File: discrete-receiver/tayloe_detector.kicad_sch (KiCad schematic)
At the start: 30 parts, among them U1 SN74CBT3253DBQR, U2 OPA1612AxD, U3 OPA1612AxD

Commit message: Fixed PCB component rotation offsets
A few components needed to get a rotation offset for JLCPCB production. Also more silkscreen content was added.
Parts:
- U1: Rotation Offset (none) -> 270
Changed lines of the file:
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@@
+			)
+		)
+		(property "Rotation Offset" "270"
+			(at 82.55 102.87 0)
+			(hide yes)
+			(show_name no)
+			(do_not_autoplace no)
+			(effects
+				(font
+					(size 1.27 1.27)
+				)
 			)
 		)

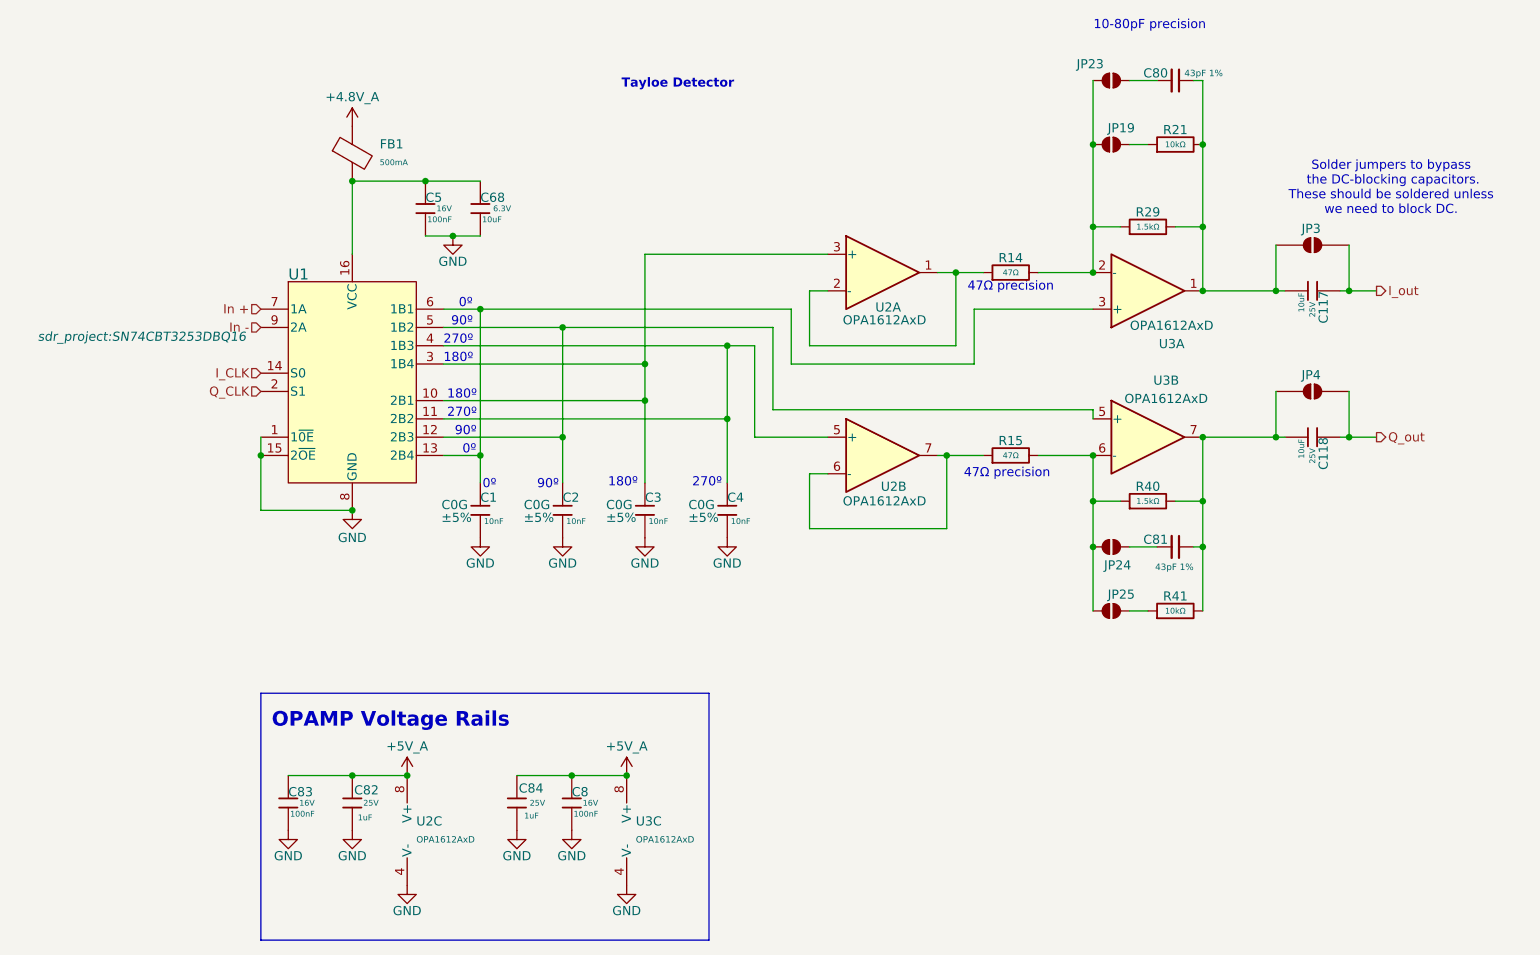
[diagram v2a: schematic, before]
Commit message: Made an edit and fixed isolated power bus in schematic&PCB
The +5V_A bus should not have been used for power in the Tayloe Detector. This was replaced with +4.8V_A in the schematic, the fix was implemented in the PCB, and that bus was connected to the +4.8V_A source.

The edit made was the making JP3 and JP4 in series with C117 & C118 rather than being in series. This change was made in both the schematic and PCB.
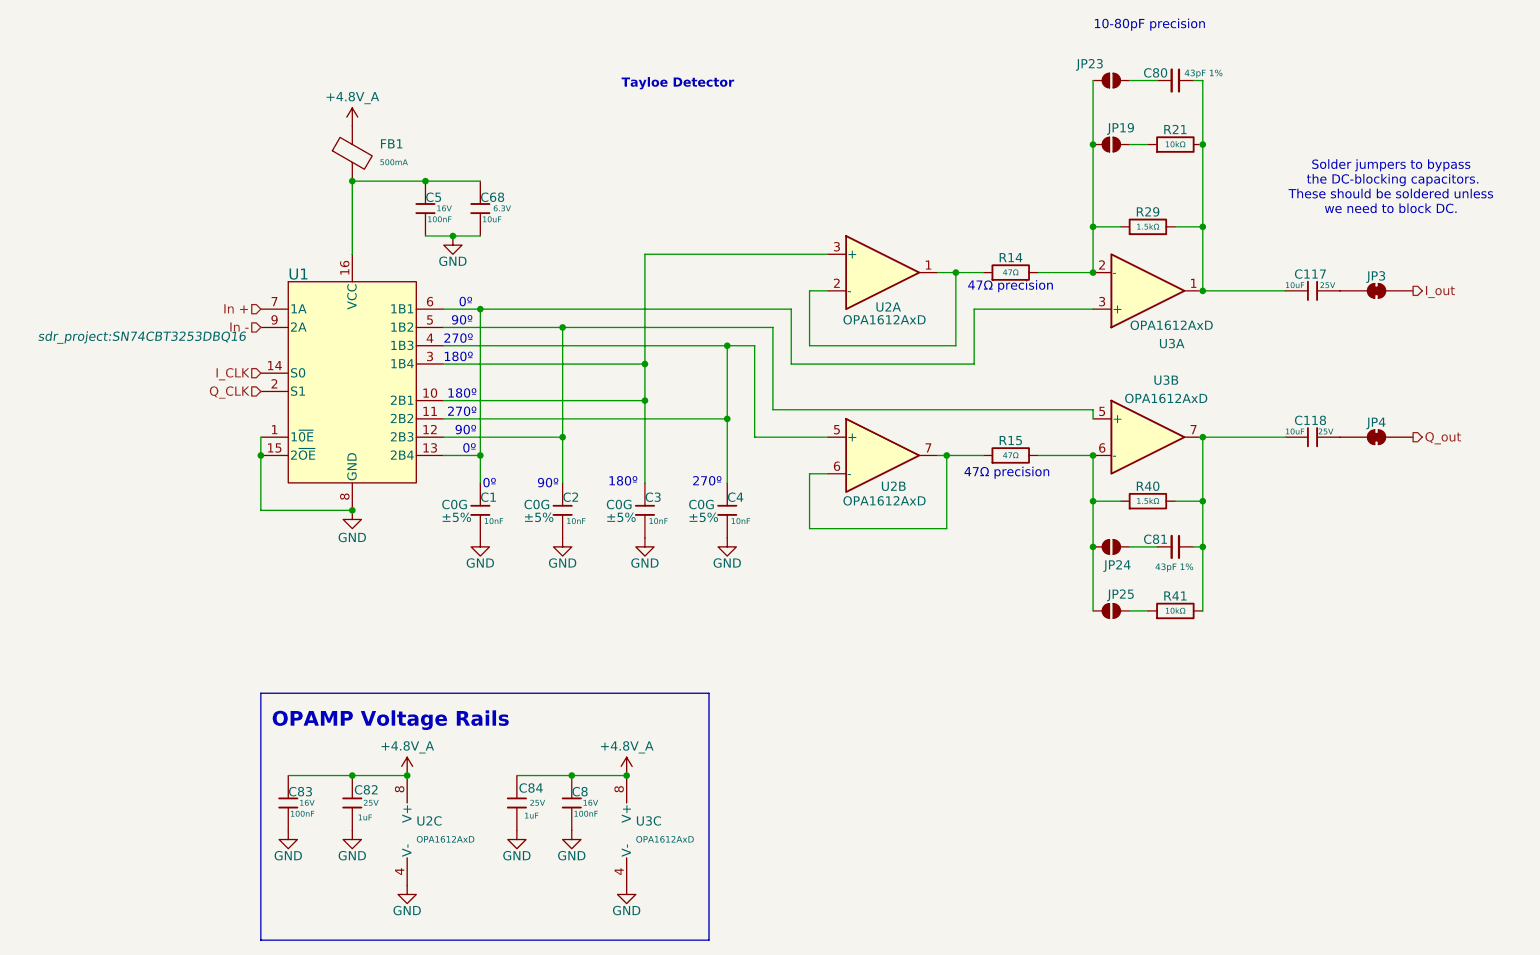
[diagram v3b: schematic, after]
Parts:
- removed JP3, JP4: SolderJumper_2_Open, Jumper:SolderJumper-2_P1.3mm_Open_Pad1.0x1.5mm, symbol Jumper:SolderJumper_2_Open
- added JP3, JP4: SolderJumper_2_Bridged, Jumper:SolderJumper-2_P1.3mm_Bridged_RoundedPad1.0x1.5mm, symbol Jumper:SolderJumper_2_Bridged
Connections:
- net +5V_A is gone; now on net +4.8V_A: C8.1, C82.1, C83.1, C84.1, U2.8 (V+), U3.8 (V+)
- net I_out: now also JP3.2 (B); no longer C117.1
- net Q_out: now also JP4.2 (B); no longer C118.1
- new net: C118.1, JP4.1 (A)
- new net: C117.1, JP3.1 (A)

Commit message: final edits before sending to JLCPCB part 1
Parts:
- removed C117, C118: 10uF, PCM_JLCPCB:C_0603, symbol PCM_JLCPCB-Capacitors:0603,10uF,(2)
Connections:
- net at C80.1, R21.2, R29.2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: now also JP3.1 (A)
- net at JP4.1 (A): now also C81.1, R40.2, R41.2, U3.7
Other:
- moved on the sheet: JP3, JP4

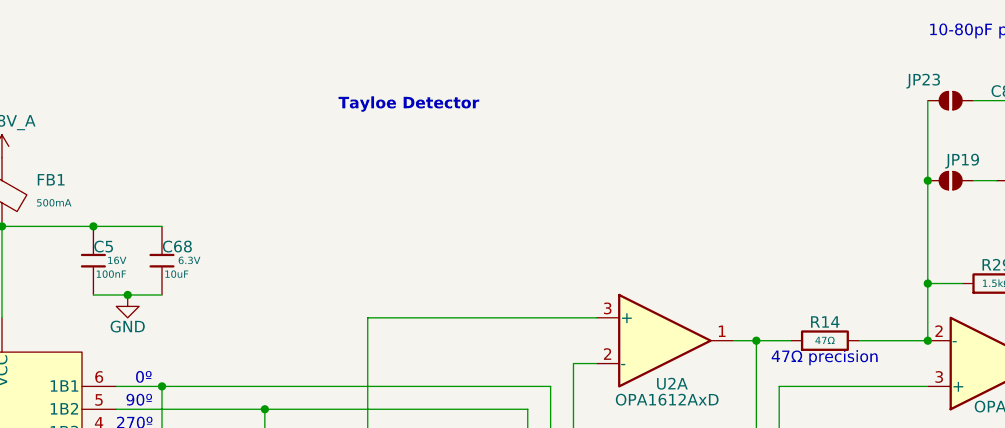
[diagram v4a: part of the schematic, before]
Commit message: Added/Modified/Deleted Schematic Notes
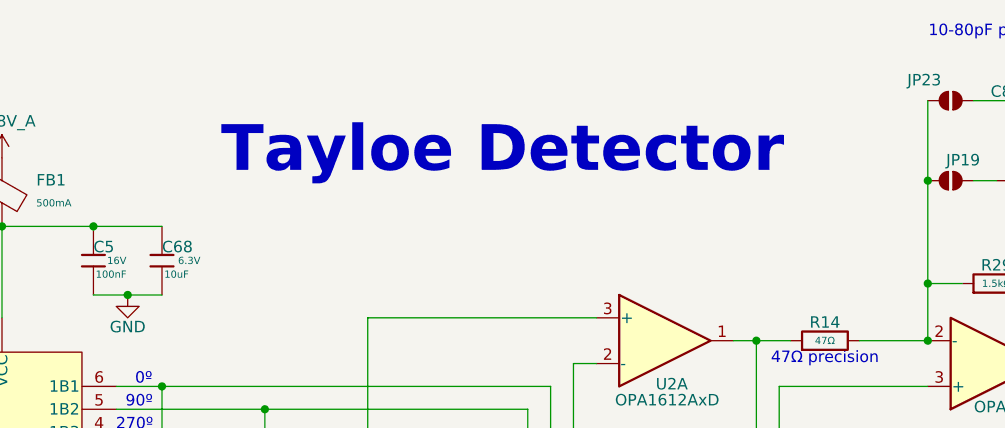
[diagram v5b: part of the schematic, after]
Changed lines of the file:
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@@
 	(text "Tayloe Detector"
 		(exclude_from_sim no)
-		(at 127.762 61.468 0)
+		(at 138.176 66.548 0)
 		(effects
 			(font
-				(size 1.27 1.27)
+				(size 5.08 5.08)
 				(thickness 0.254)
 				(bold yes)
